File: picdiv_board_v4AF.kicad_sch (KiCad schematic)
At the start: 58 parts, among them J1 DC-Input, J10 PPS_B, J11 PPS_B, J2 MountingHole_M2.5, J3 MountingHole_M2.5, J4 TEST_1PPS, J5 Conn_01x06, J6 Sync, J7 Sync, J8 10MHz, J9 10MHz, SW1 SW_DIP_x03, U1 LT1963AEST-3.3, U2 LT1963AEST-3.3, U3 PIC12F675-xSN, U4 NE555D, U5 IDT5PB1108, U6 IDT5PB1108

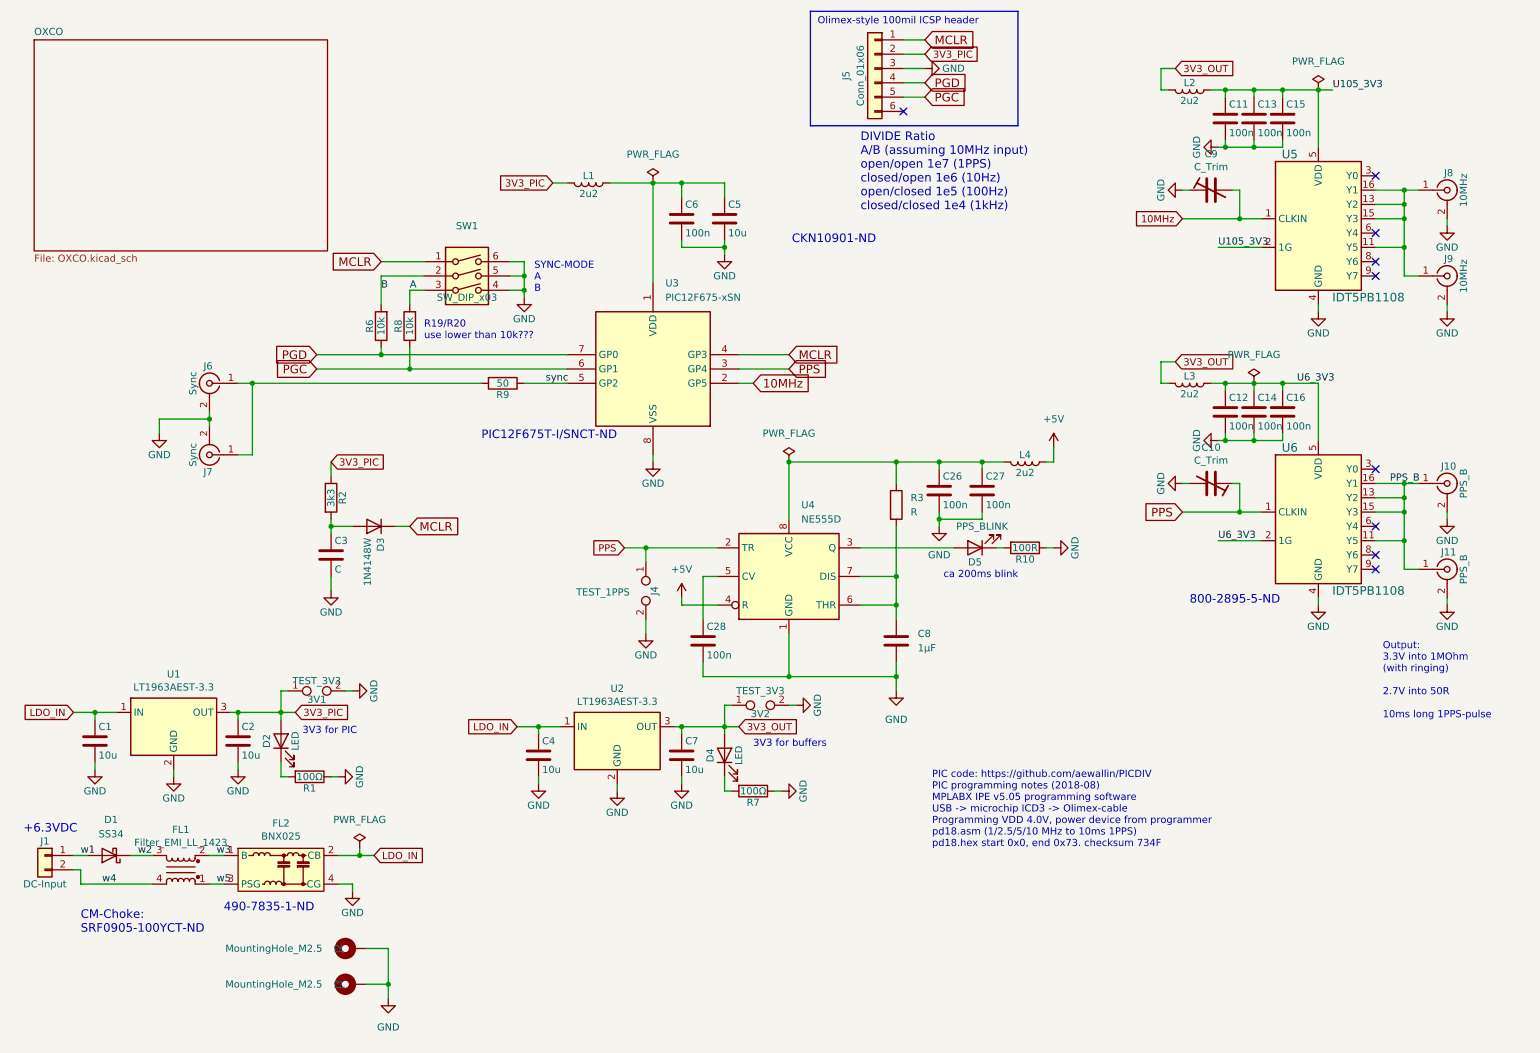
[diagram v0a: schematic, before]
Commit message: Add inverter to 555 input.
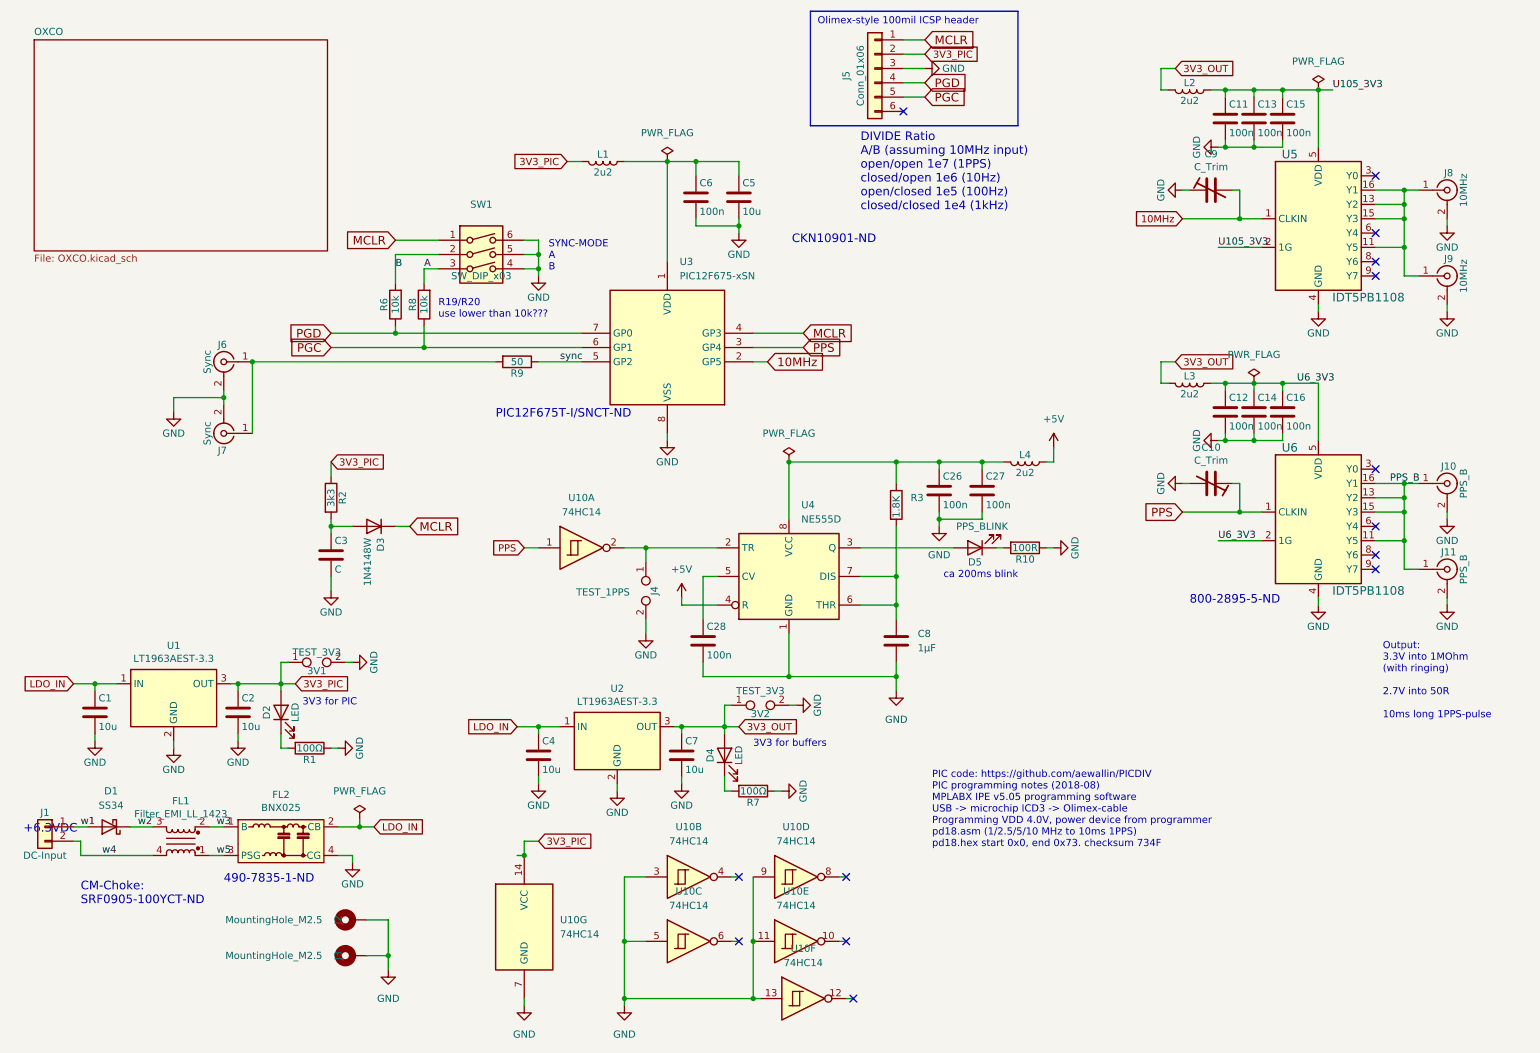
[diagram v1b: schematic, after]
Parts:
- added U10: 74HC14, Package_SO:SOIC-14_3.9x8.7mm_P1.27mm, symbol 74xx:74HC14
- R3: value R -> 1.8K; LCSC (none) -> 0805W8F1801T5E; MPN (none) -> 0805W8F1801T5E
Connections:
- net 3V3_PIC: now also U10.14 (VCC)
- net GND: now also U10.11, U10.13, U10.3, U10.5, U10.7 (GND), U10.9
- net PPS: now also U10.1; no longer J4.1, U4.2 (TR)
- new net: J4.1, U10.2, U4.2 (TR)
- no-connect marks 9 -> 14
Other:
- moved on the sheet: 3V1, C1, C2, C5, C6, D1, D2, FL1, FL2, J1, J2, J3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

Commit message: 555 stuff
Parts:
- C3: value C -> 100n; LCSC (none) -> C49678
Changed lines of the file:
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@@
 			)
 		)
-		(property "Value" "C"
+		(property "Value" "100n"
 			(at 71.755 113.03 0)
 			(effects
@@
 			(at 71.12 110.49 0)
 			(effects
+				(font
+					(size 1.27 1.27)
+				)
+				(hide yes)
+			)
+		)
+		(property "MPN" ""
+			(at 71.12 110.49 0)
+			(effects
+				(font
+					(size 1.27 1.27)
+				)
+				(hide yes)
+			)
+		)
+		(property "LCSC" "C49678"
+			(at 71.12 110.49 0)
+			(effects

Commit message: 555
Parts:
- added C29: 100n, Capacitor_SMD:C_0805_2012Metric, symbol Device:C
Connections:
- net 3V3_PIC: now also C29.1
- net GND: now also C29.2
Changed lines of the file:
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@@
 	)
 	(junction
+		(at 105.41 189.23)
+		(diameter 0)
+		(color 0 0 0 0)
+	)
+	(junction
 		(at 240.03 80.01)
 		(diameter 0)
@@
 	(wire
 		(pts
+			(xy 92.71 189.23) (xy 105.41 189.23)
+		)
+		(stroke
+			(width 0)
+			(type default)
+		)
+	)
+	(wire
+		(pts
 			(xy 76.2 158.75) (xy 78.74 158.75)
 		)
@@
 	(wire
 		(pts
-			(xy 105.41 163.83) (xy 104.14 163.83)
-		)
-		(stroke
-			(width 0)
-			(type default)
-		)
-	)
-	(wire
-		(pts
 			(xy 105.41 59.69) (xy 107.95 59.69)
 		)
@@
 	(wire
 		(pts
+			(xy 92.71 163.83) (xy 92.71 172.72)
+		)
+		(stroke
+			(width 0)
+			(type default)
+		)
+	)
+	(wire
+		(pts
 			(xy 62.23 133.35) (xy 62.23 134.62)
 		)
@@
 	(wire
 		(pts
+			(xy 92.71 163.83) (xy 105.41 163.83)
+		)
+		(stroke
+			(width 0)
+			(type default)
+		)
+	)
+	(wire
+		(pts
 			(xy 107.95 59.69) (xy 107.95 60.96)
 		)
@@
 	(wire
 		(pts
+			(xy 92.71 180.34) (xy 92.71 189.23)
+		)
+		(stroke
+			(width 0)
+			(type default)
+		)
+	)
+	(wire
+		(pts
 			(xy 256.54 102.87) (xy 261.62 102.87)
 		)
@@
 					(unit 1)
 				)
+			)
+		)
+	)
+	(symbol
+		(lib_id "Device:C")
+		(at 92.71 176.53 0)
+		(unit 1)
+		(exclude_from_sim no)
+		(in_bom yes)
+		(on_board yes)
+		(dnp no)
+		(property "Reference" "C29"
+			(at 93.345 173.99 0)
+			(effects
+				(font
+					(size 1.27 1.27)
+				)
+				(justify left)
+			)
+		)
+		(property "Value" "100n"
+			(at 93.345 179.07 0)
+			(effects
+				(font
+					(size 1.27 1.27)
+				)
+				(justify left)
+			)
+		)
+		(property "Footprint" "Capacitor_SMD:C_0805_2012Metric"
+			(at 93.6752 180.34 0)
+			(effects
+				(font
+					(size 1.27 1.27)
+				)
+				(hide yes)
+			)
+		)
+		(property "Datasheet" "~"
+			(at 92.71 176.53 0)
+			(effects
+				(font
+					(size 1.27 1.27)
+				)
+				(hide yes)
+			)
+		)
+		(property "Description" "Unpolarized capacitor"
+			(at 92.71 176.53 0)
+			(effects
+				(font
+					(size 1.27 1.27)
+				)
+				(hide yes)
+			)
+		)
+		(property "MPN" "CC0805KRX7R9BB104"
+			(at 92.71 176.53 0)
+			(effects
+				(font
+					(size 1.27 1.27)
+				)
+				(hide yes)
+			)
+		)
+		(property "LCSC" "C49678"
+			(at 92.71 176.53 0)
+			(effects
+				(font
+					(size 1.27 1.27)
+				)
+				(hide yes)
+			)
+		)
+		(pin "1"
+		)
+		(pin "2"
+		)
+		(instances
+			(project "picdiv_board_v4AF"
+				(path "/eba36321-b5f3-4bd6-a805-57b9b2ee447e"
+					(reference "C29")
+					(unit 1)
+				)

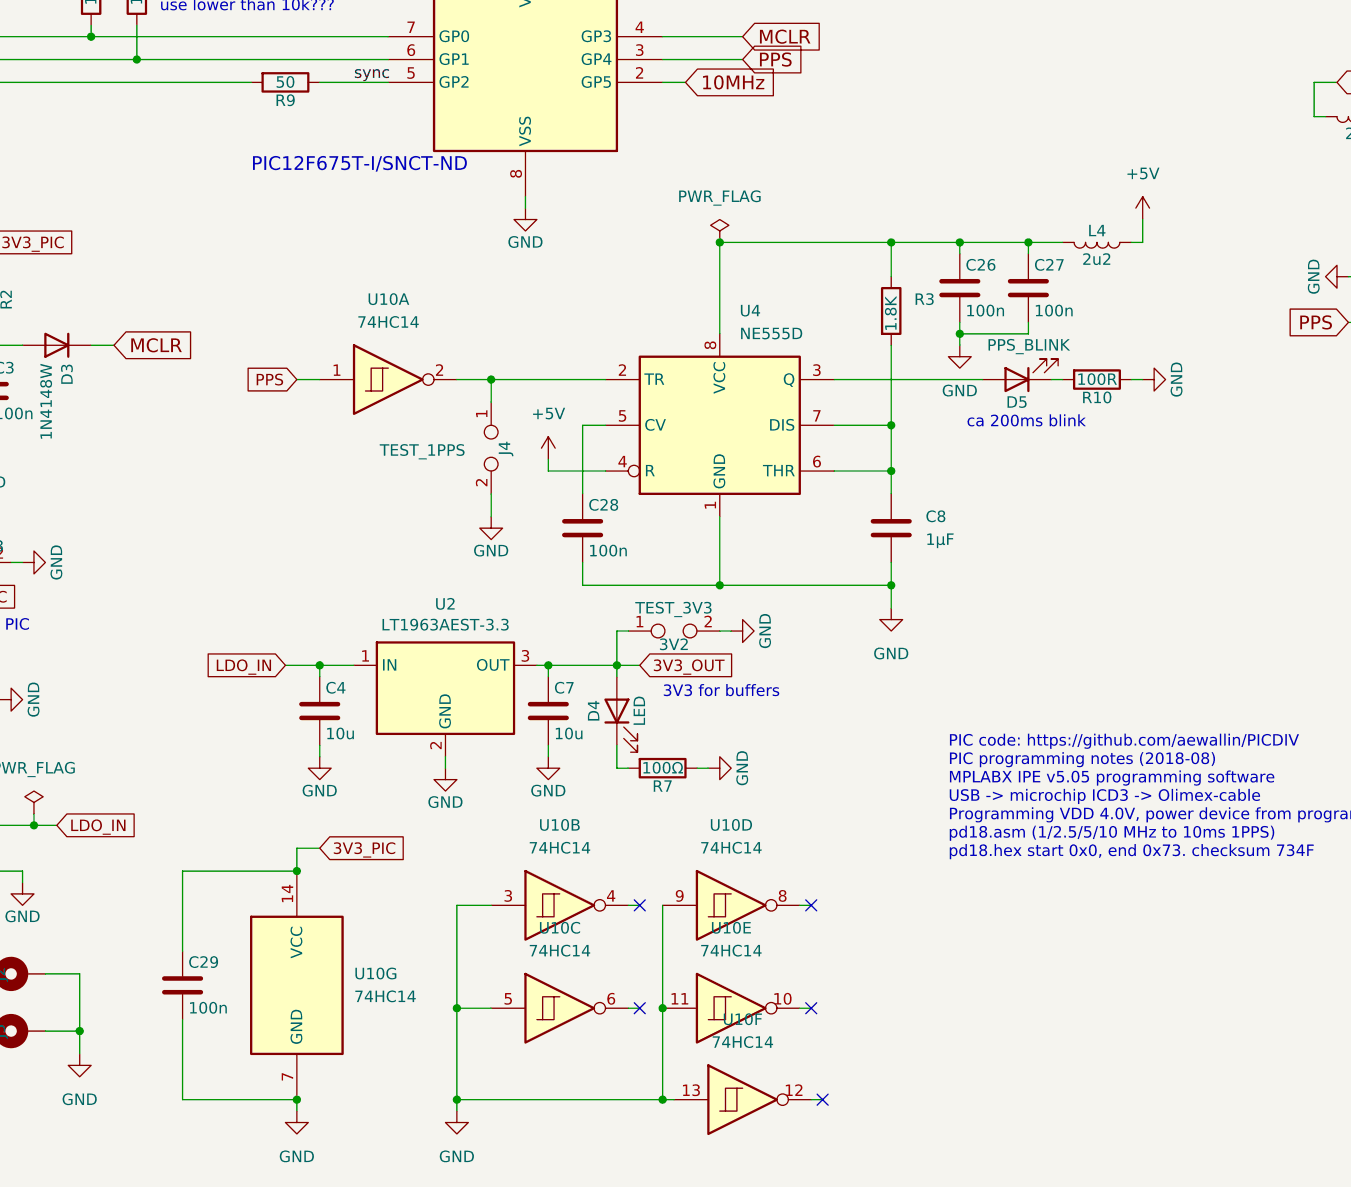
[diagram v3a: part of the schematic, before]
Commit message: Start fixing JLC design rule violations. There over 100 left.
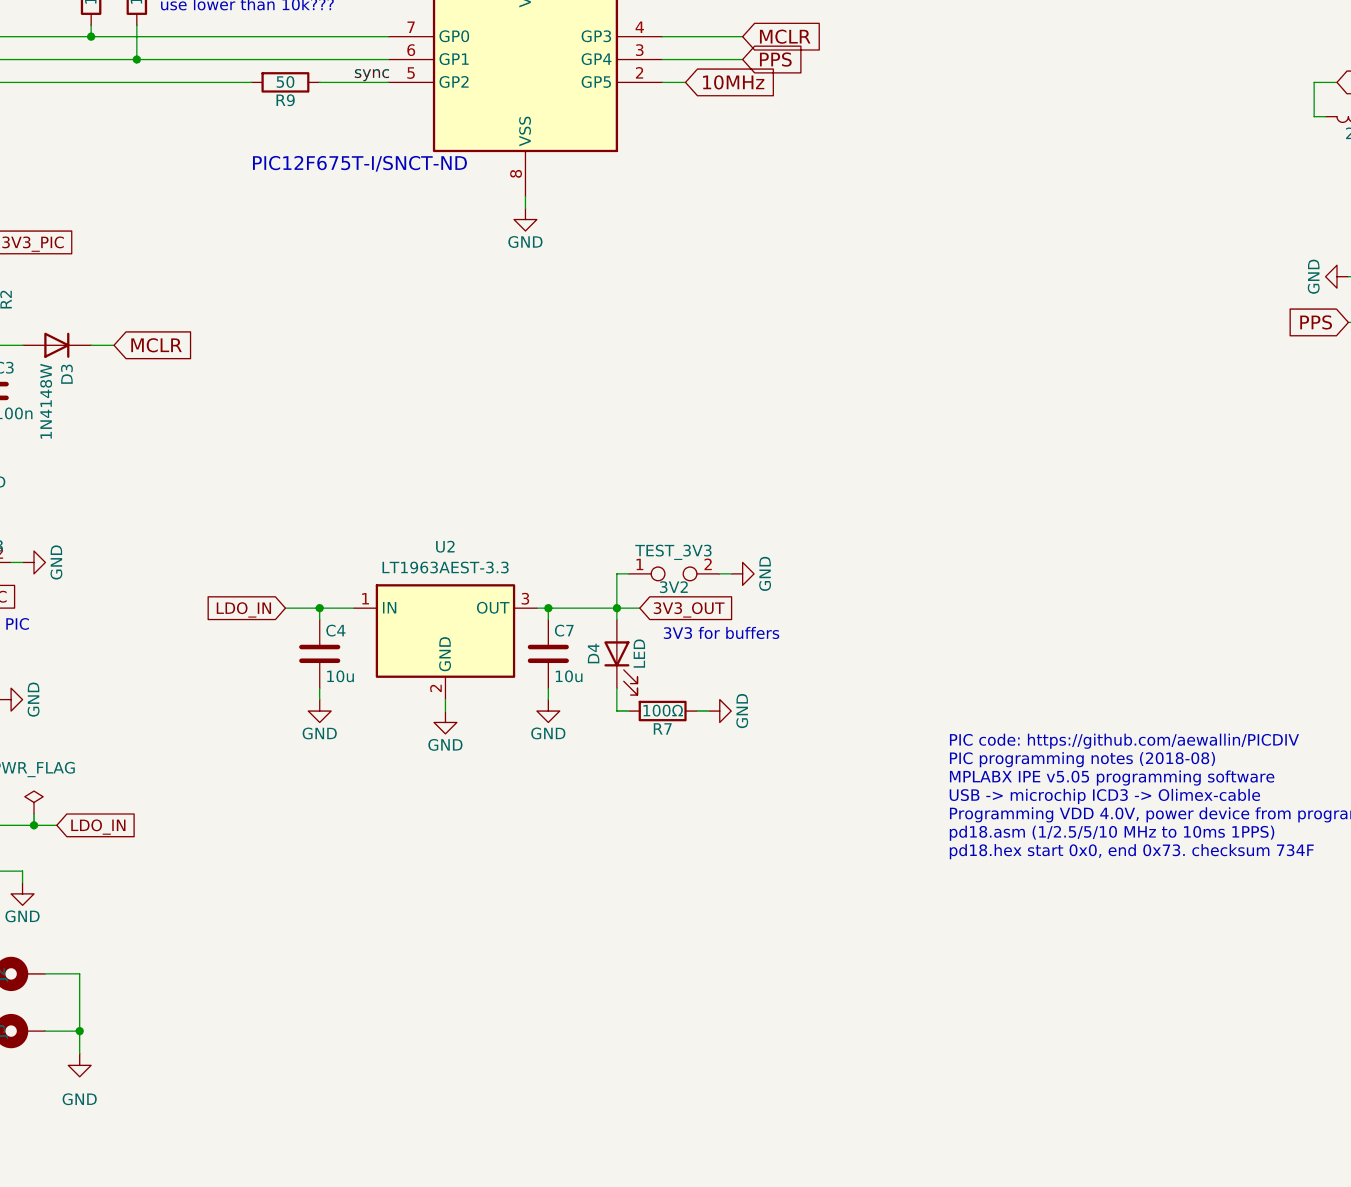
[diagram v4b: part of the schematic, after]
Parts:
- removed C26, C27, C28, C29: 100n, Capacitor_SMD:C_0805_2012Metric, symbol Device:C
- removed C8: 1µF, Capacitor_SMD:C_0805_2012Metric, symbol Device:C
- removed D5: PPS_BLINK, LED_SMD:LED_0805_2012Metric, symbol Device:LED
- removed J4: TEST_1PPS, TestPoint:TestPoint_2Pads_Pitch2.54mm_Drill0.8mm, symbol Connector:TestPoint_2Pole
- removed L4: 2u2, Inductor_SMD:L_0805_2012Metric, symbol Device:L
- removed R10: 100R, Resistor_SMD:R_0805_2012Metric, symbol Device:R
- removed R3: 1.8K, Resistor_SMD:R_0805_2012Metric, symbol Device:R
- removed U10: 74HC14, Package_SO:SOIC-14_3.9x8.7mm_P1.27mm, symbol 74xx:74HC14
- removed U4: NE555D, Package_SO:SOIC-8_3.9x4.9mm_P1.27mm, symbol Timer:NE555D
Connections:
- no-connect marks 14 -> 9
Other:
- note removed: "ca 200ms blink"
- moved on the sheet: 3V2, C4, C7, D4, R7, U2

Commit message: Highlight a DRC error
Needs  more work.
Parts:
- D3: footprint Diodes_SMD:D_SOD-123 -> Diode_SMD:D_SOD-123
